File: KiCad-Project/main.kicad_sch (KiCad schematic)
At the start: 32 parts, among them J1 USB_C_Receptacle_USB2.0, J2 BAT, J3 JTAG_TC2030, J4 RST, U1 nRF52840_moko_mk08, U2 SRV05-4, U3 MAX17048, U4 BQ24075RGT

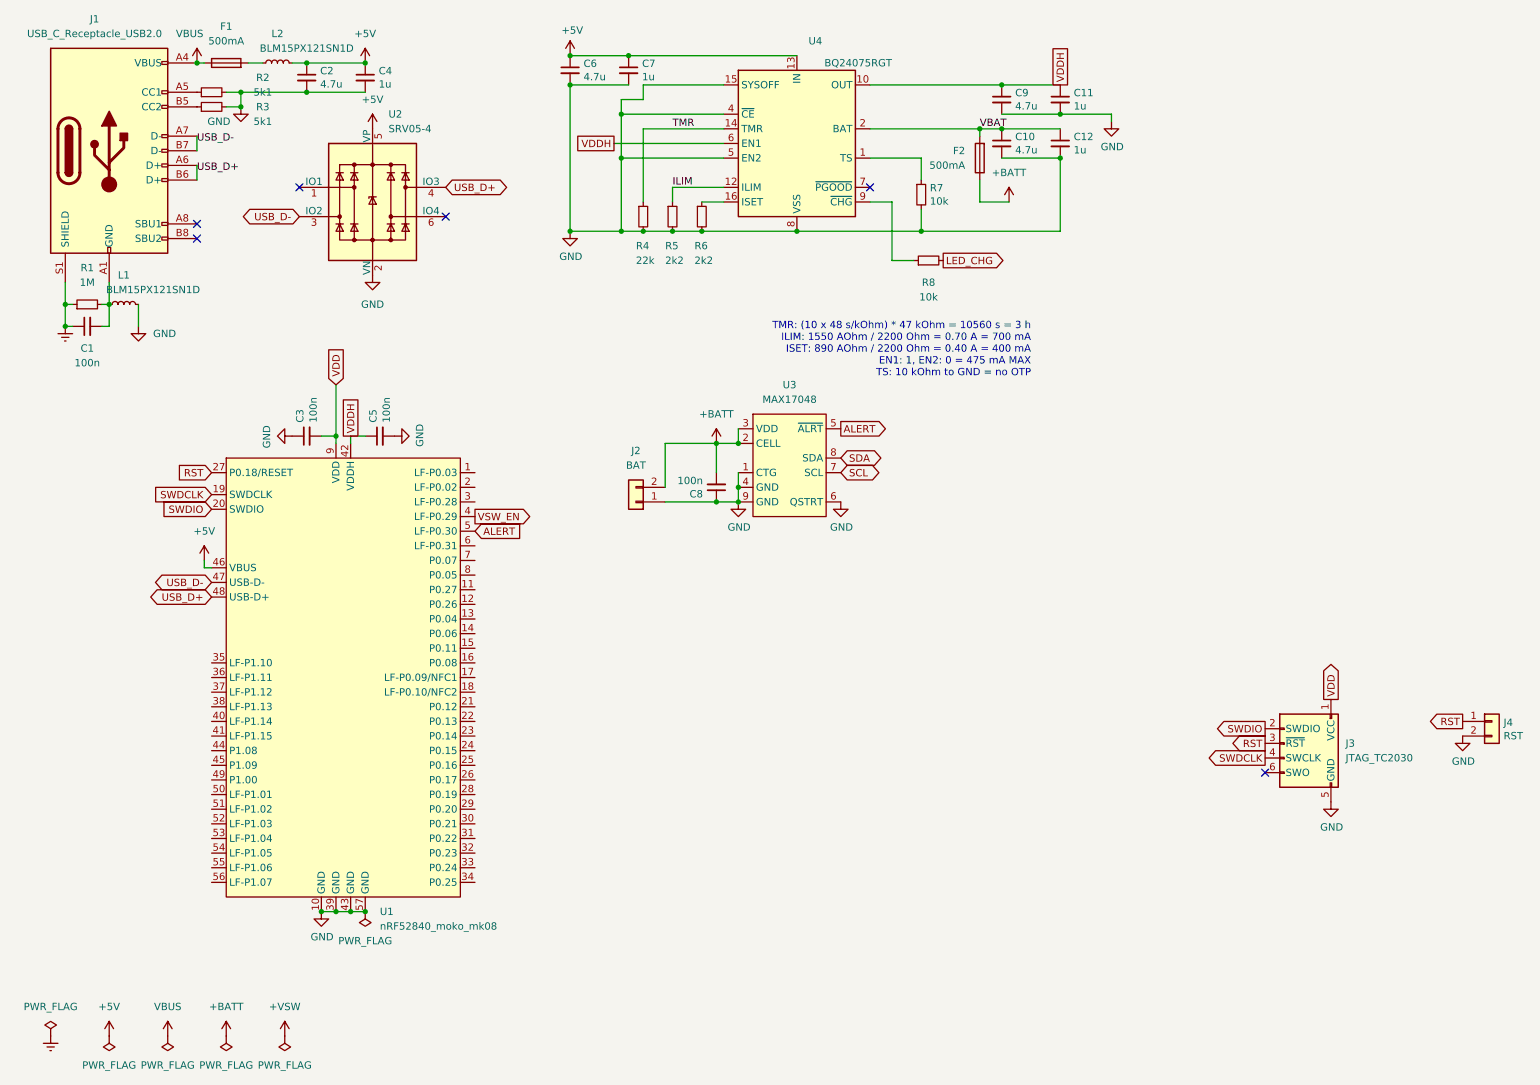
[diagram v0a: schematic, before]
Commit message: finish routing the matrix
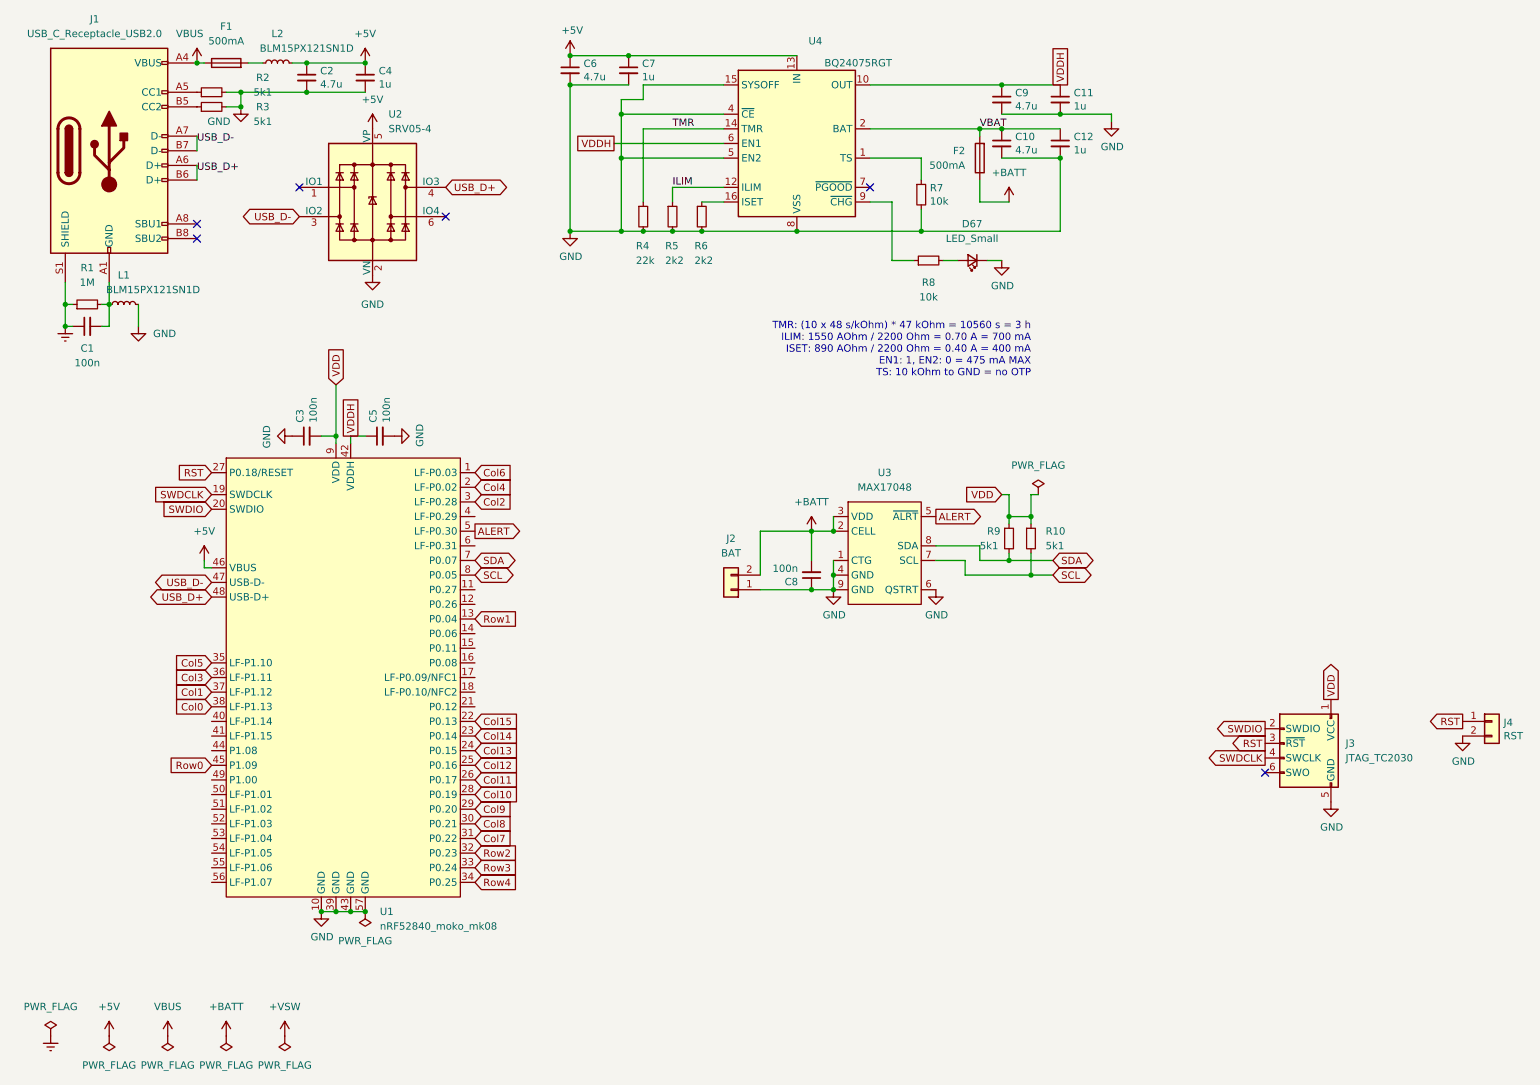
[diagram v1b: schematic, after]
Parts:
- added D67: LED_Small, LED_SMD:LED_0603_1608Metric, symbol Device:LED_Small
- added R10, R9: 5k1, Resistor_SMD:R_0402_1005Metric, symbol Device:R_Small
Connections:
- net GND: now also D67.1 (K)
- net SCL: now also U1.8 (P0.05), R10.2
- net SDA: now also U1.7 (P0.07), R9.2
- net VDD: now also R10.1, R9.1
- net Col6: now reaches U1.1 (LF-P0.03)
- net Row1: now reaches U1.13 (P0.04)
- net Col4: now reaches U1.2 (LF-P0.02)
- net Col15: now reaches U1.22 (P0.13)
- net Col14: now reaches U1.23 (P0.14)
- net Col13: now reaches U1.24 (P0.15)
- net Col12: now reaches U1.25 (P0.16)
- net Col11: now reaches U1.26 (P0.17)
- net Col10: now reaches U1.28 (P0.19)
- net Col9: now reaches U1.29 (P0.20)
- net Col2: now reaches U1.3 (LF-P0.28)
- net Col8: now reaches U1.30 (P0.21)
- net Col7: now reaches U1.31 (P0.22)
- net Row2: now reaches U1.32 (P0.23)
- net Row3: now reaches U1.33 (P0.24)
- net Row4: now reaches U1.34 (P0.25)
- net Col5: now reaches U1.35 (LF-P1.10)
- net Col3: now reaches U1.36 (LF-P1.11)
- net Col1: now reaches U1.37 (LF-P1.12)
- net Col0: now reaches U1.38 (LF-P1.13)
- net Row0: now reaches U1.45 (P1.09)
- net LED_CHG: no longer names the net of R8.2
- net LED_CHG: now also D67.2 (A)
- net VSW_EN: no longer names the net of U1.4 (LF-P0.29)

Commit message: Finish routing PCB
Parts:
- added D68, D69, D70: LED_Small, LED_THT:LED_D3.0mm, symbol Device:LED_Small
- added R11, R12, R13: 1k, Resistor_SMD:R_0402_1005Metric, symbol Device:R_Small
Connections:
- net GND: now also D68.1 (K), D69.1 (K), D70.1 (K)
- net Num: now reaches U1.54 (LF-P1.05)
- net Num: now also R12.1
- net Scroll: now reaches U1.55 (LF-P1.06)
- net Scroll: now also R13.1
- net Caps: now reaches U1.56 (LF-P1.07)
- net Caps: now also R11.1
- new net: D69.2 (A), R12.2
- new net: D68.2 (A), R11.2
- new net: D70.2 (A), R13.2
